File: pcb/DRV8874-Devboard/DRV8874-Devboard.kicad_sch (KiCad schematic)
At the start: 53 parts, among them J1 Conn_01x04_Pin, J10 Conn_01x06_Pin, J12 Conn_01x03_Pin, J2 Screw_Terminal_01x02, J3 Conn_01x03_Pin, J4 Conn_01x03_Pin, J5 Conn_01x04_Pin, J6 Conn_01x03_Pin, J7 Conn_01x03_Pin, J9 Conn_01x03_Pin, U1 DRV8874, U2 BL9342, U3 DRV8874, U4 SN65HVD230, U5 TPS16630PWPR, U6 M95320-WMN6TP, U7 TinyThinker_J1

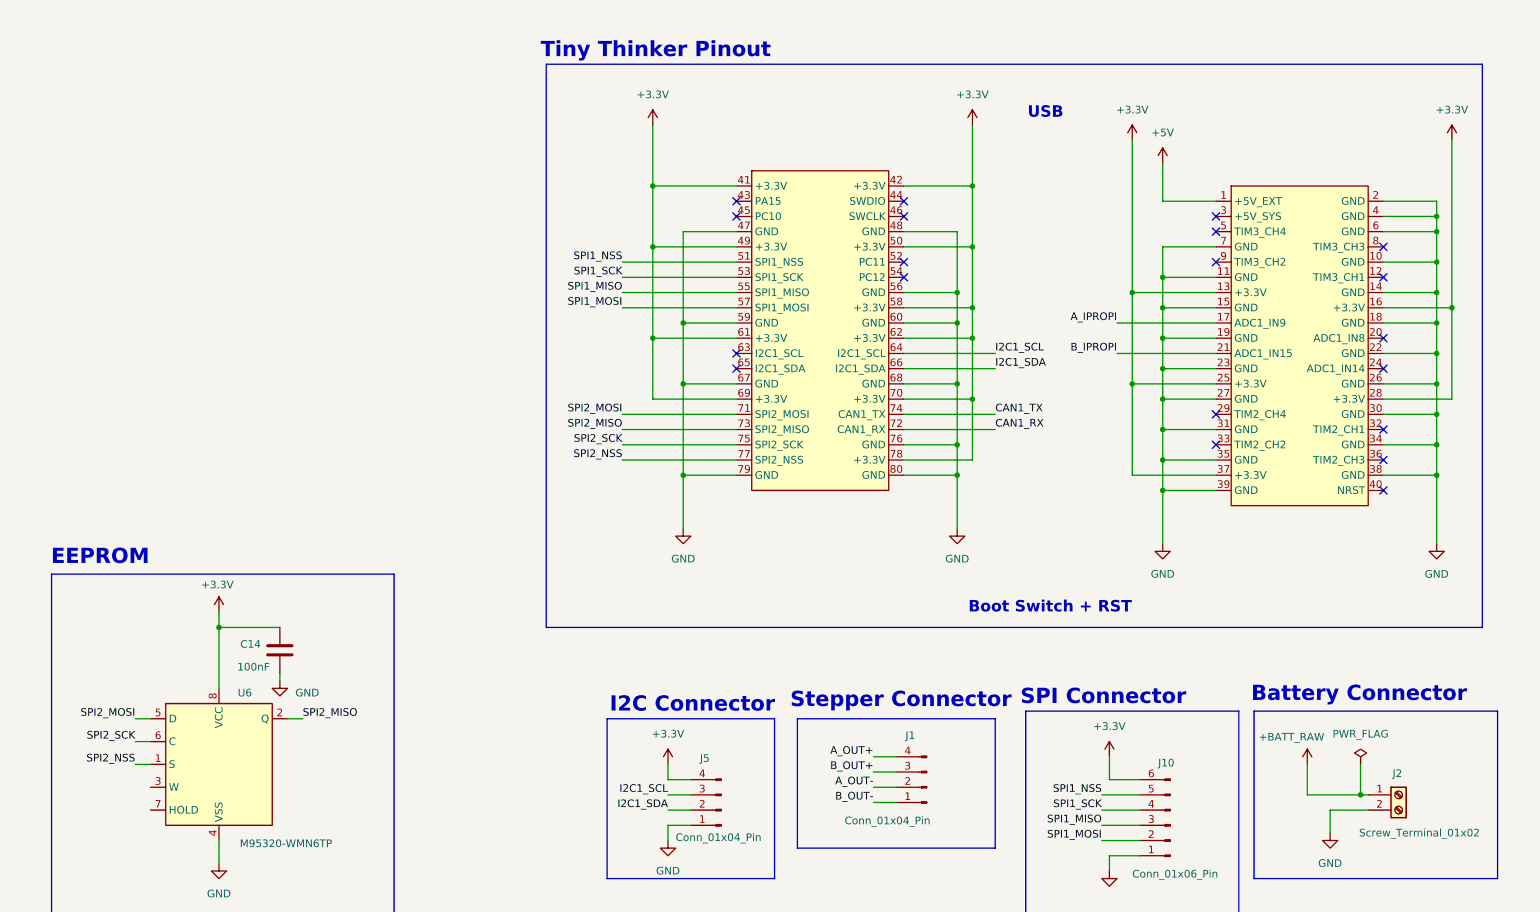
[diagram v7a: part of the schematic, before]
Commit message: routed major chunk of DRV8874 pair
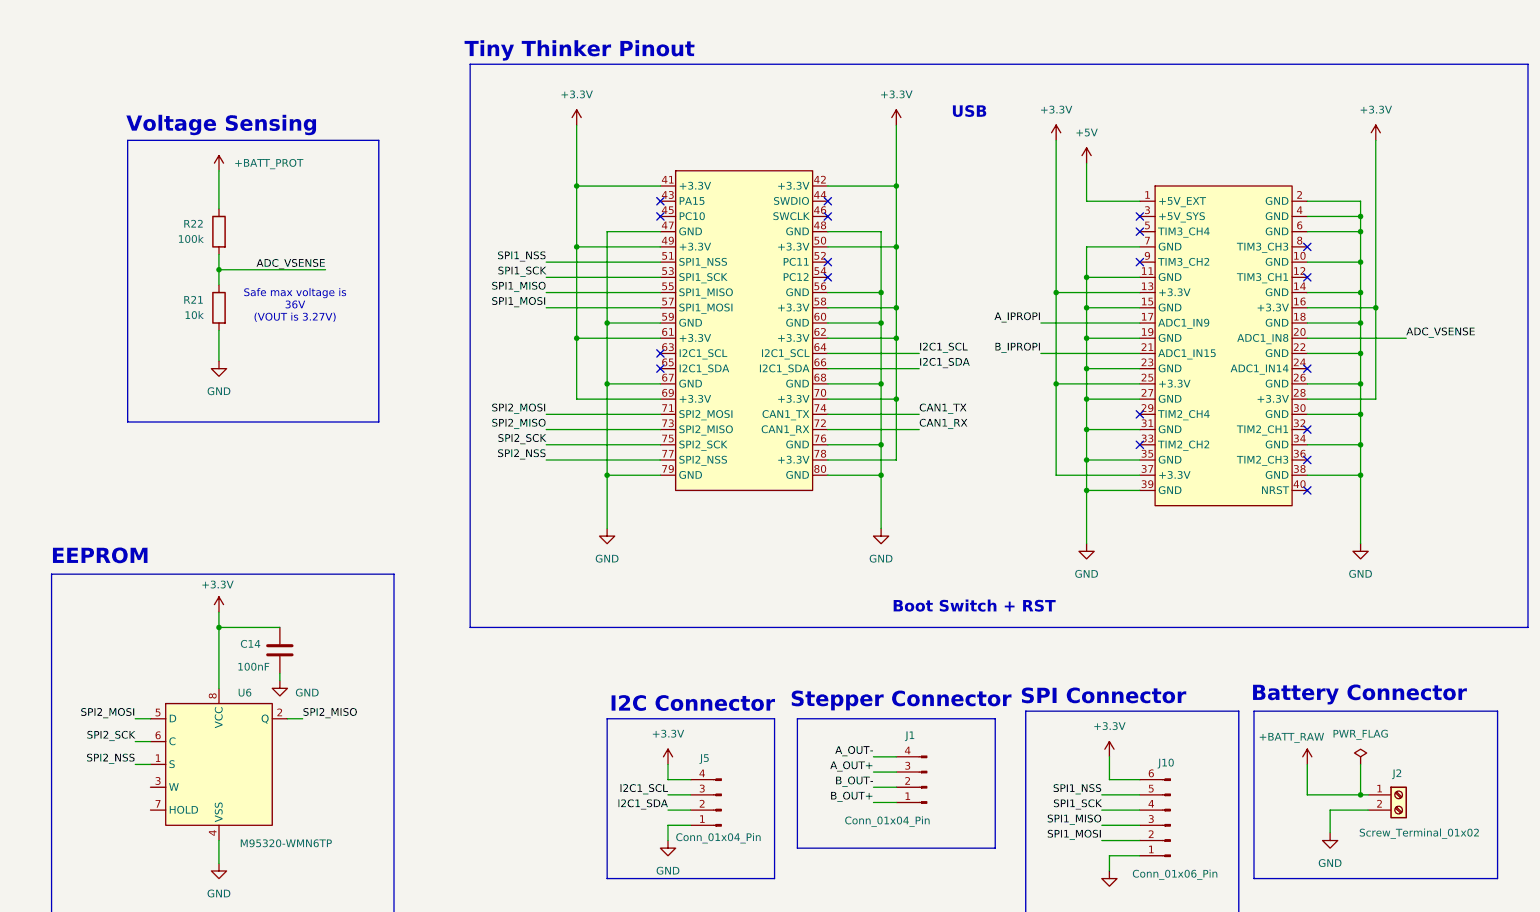
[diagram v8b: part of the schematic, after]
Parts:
- added R21: 10k, Resistor_SMD:R_0402_1005Metric, symbol Device:R
- added R22: 100k, Resistor_SMD:R_0603_1608Metric, symbol Device:R
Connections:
- net +BATT_PROT: now also R22.1
- net A_OUT+: now also J1.3 (Pin_3); no longer J1.4 (Pin_4)
- net A_OUT-: now also J1.4 (Pin_4); no longer J1.2 (Pin_2)
- net B_OUT+: now also J1.1 (Pin_1); no longer J1.3 (Pin_3)
- net B_OUT-: now also J1.2 (Pin_2); no longer J1.1 (Pin_1)
- net GND: now also R21.2
- net ADC_VSENSE: now reaches U7.20 (ADC1_IN8)
- net ADC_VSENSE: now also R21.1, R22.2
- no-connect marks 23 -> 22
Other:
- note added: "Safe max voltage is 36V (VOUT is 3.27V)"
- note added: "Voltage Sensing"
